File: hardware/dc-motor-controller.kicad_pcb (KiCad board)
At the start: 2 copper layers, 52.2 x 85 mm, 30 parts, among them IC1 ATMEGA88PA-P, M1 DC_motor, M2 DC_motor, M3 DC_motor, P1 Power connector, P2 ISP interface, SW1 SW_PUSH, SW2 SW_PUSH, SW3 SW_PUSH, SW4 SW_PUSH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

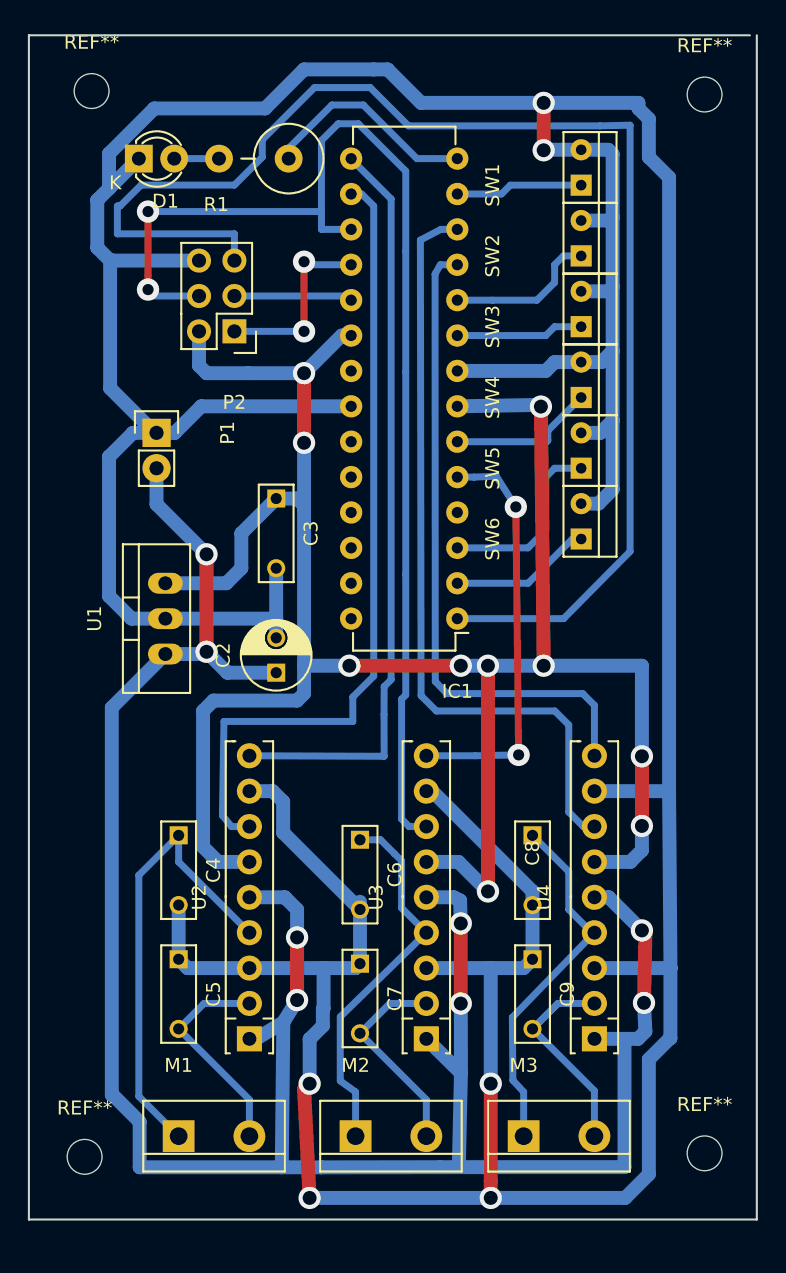
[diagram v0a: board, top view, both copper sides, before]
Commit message: Some changes after reviewing the printed circuit board
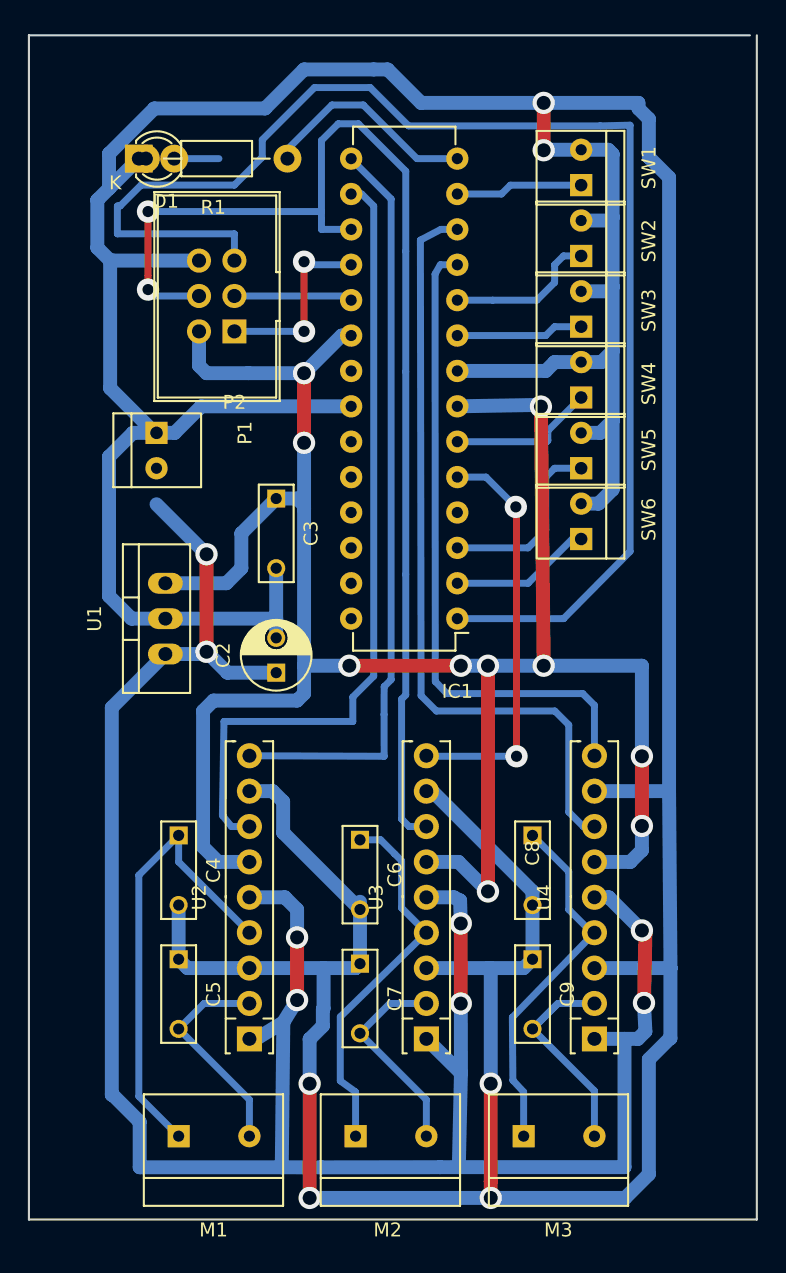
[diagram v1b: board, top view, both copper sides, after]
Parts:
- removed REF** (x4): MountingHole_2-5mm, Mounting_Holes:MountingHole_2-5mm
- M1, M2, M3: footprint Oturpe footprints:Big_green_chocolade_1x2 -> Oturpe footprints:Big_green_chocolate_1x2
- P1: footprint Socket_Strips:Socket_Strip_Straight_1x02 -> Oturpe footprints:Small_green_chocolade_1x2
- P2: footprint Pin_Headers:Pin_Header_Straight_2x03 -> Oturpe footprints:Borg_hedged_2x03
- R1: footprint Resistors_ThroughHole:Resistor_Vertical_RM5mm -> Resistors_ThroughHole:Resistor_Horizontal_RM10mm
- moved R1 2.41 mm to (114.8, 101.6)
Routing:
- net +12V: track 173.1 -> 170.5 mm

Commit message: Improved part numbering of schematic
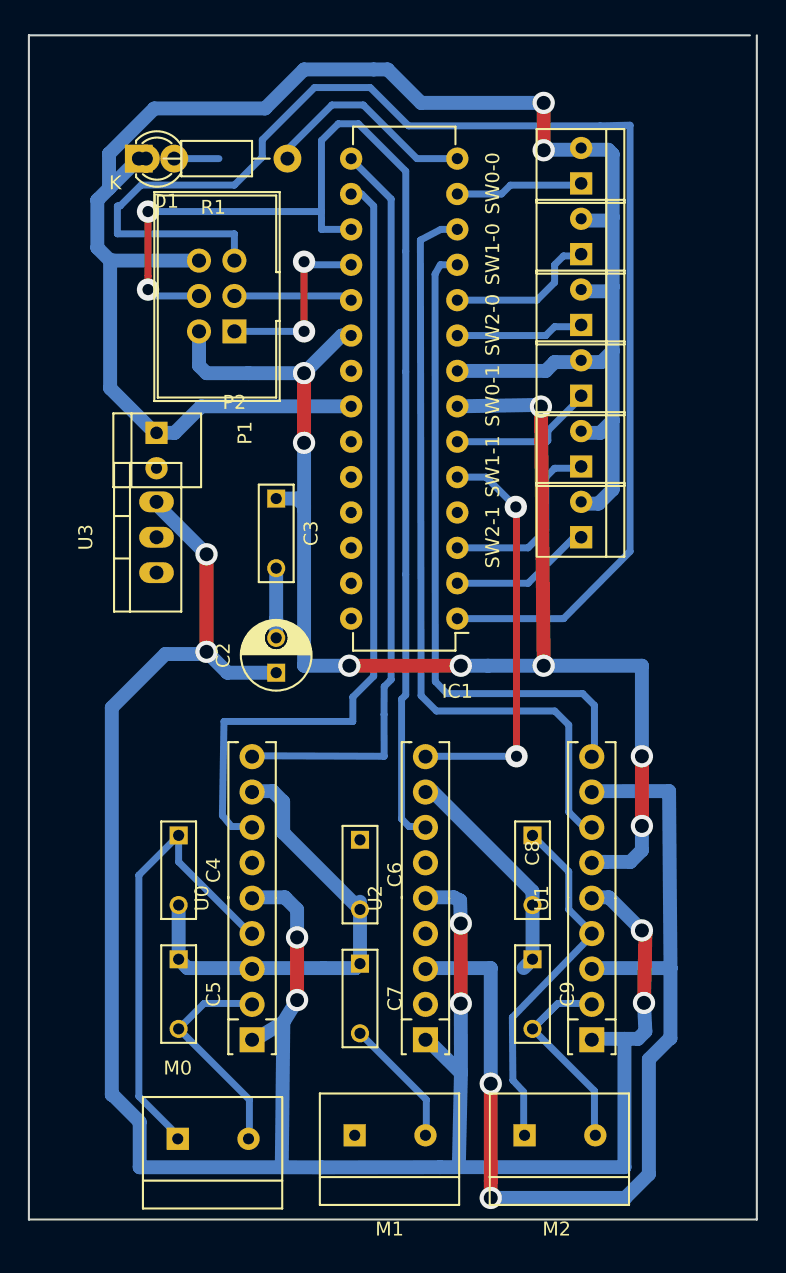
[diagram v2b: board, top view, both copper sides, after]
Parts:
- removed M3: DC_motor, Oturpe footprints:Big_green_chocolate_1x2
- removed SW1, SW2, SW3, SW4, SW5, SW6: SW_PUSH, Oturpe footprints:Small_green_chocolade_1x2
- removed U4: BA6956AN, Housings_SIP:SIP9_Housing
- added M0: DC_motor, Oturpe footprints:Big_green_chocolate_1x2, F.Cu at (106.9, 172.0)
- added SW0-0: SW_PUSH, Oturpe footprints:Small_green_chocolade_1x2, F.Cu at (135.9, 103.4)
- added SW0-1: SW_PUSH, Oturpe footprints:Small_green_chocolade_1x2, F.Cu at (135.9, 118.6)
- added SW1-0: SW_PUSH, Oturpe footprints:Small_green_chocolade_1x2, F.Cu at (135.9, 108.5)
- added SW1-1: SW_PUSH, Oturpe footprints:Small_green_chocolade_1x2, F.Cu at (135.9, 123.7)
- added SW2-0: SW_PUSH, Oturpe footprints:Small_green_chocolade_1x2, F.Cu at (135.9, 113.5)
- added SW2-1: SW_PUSH, Oturpe footprints:Small_green_chocolade_1x2, F.Cu at (135.9, 128.8)
- added U0: BA6956AN, Housings_SIP:SIP9_Housing, F.Cu at (112.3, 154.7)
- U1: value 7805 -> BA6956AN; footprint TO_SOT_Packages_THT:TO-220_Neutral123_Vertical -> Housings_SIP:SIP9_Housing
- U3: value BA6956AN -> 7805; footprint Housings_SIP:SIP9_Housing -> TO_SOT_Packages_THT:TO-220_Neutral123_Vertical
- moved U1 36.6 mm to (136.7, 154.7)
- moved U3 32.3 mm to (105.4, 128.8)
- moved M1 12.6 mm to (119.6, 171.7)
- moved U2 12.6 mm to (124.7, 154.7)
- moved M2 12.1 mm to (131.8, 171.7)
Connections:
- IC1 pad 11: Net-(IC1-Pad11) -> /M0R
- IC1 pad 12: Net-(IC1-Pad12) -> /M0F
- IC1 pad 15: Net-(IC1-Pad15) -> /M1F
- IC1 pad 16: Net-(IC1-Pad16) -> /M1R
- IC1 pad 17: Net-(IC1-Pad17) -> /M2R
- IC1 pad 5: Net-(IC1-Pad5) -> /M2R
- M1 pad 1: Net-(C4-Pad1) -> Net-(C6-Pad1)
- M1 pad 2: Net-(C5-Pad2) -> Net-(C7-Pad2)
- M2 pad 1: Net-(C6-Pad1) -> Net-(C8-Pad1)
- M2 pad 2: Net-(C7-Pad2) -> Net-(C9-Pad2)
- P2 pad 4: Net-(IC1-Pad17) -> /M2R
- U1 pad 1: +12V -> (no net)
- U1 pad 2: GND -> Net-(C7-Pad2)
- U1 pad 3: +5V -> GND
- U2 pad 1: +12V -> (no net)
- U2 pad 2: Net-(C5-Pad2) -> Net-(C9-Pad2)
- U2 pad 4: Net-(C4-Pad1) -> Net-(C8-Pad1)
- U2 pad 6: +5V -> +12V
- U2 pad 7: Net-(IC1-Pad16) -> (no net)
- U2 pad 9: Net-(IC1-Pad15) -> /M2R
- U3 pad 2: Net-(C7-Pad2) -> GND
- U3 pad 3: GND -> +5V
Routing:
- net /M2R: track 0.00 -> 116.9 mm, vias 0 -> 4
- net GND: track 380.4 -> 263.9 mm, vias 6 -> 4
- net /M0R: track 0.00 -> 93.3 mm
- net Net-(IC1-Pad17): track 87.4 -> 0.00 mm, vias 2 -> 0
- net /M0F: track 0.00 -> 58.8 mm
- net Net-(IC1-Pad16): track 57.9 -> 0.00 mm
- net /M1F: track 0.00 -> 56.8 mm
- net Net-(IC1-Pad12): track 55.5 -> 0.00 mm
- net Net-(IC1-Pad15): track 54.0 -> 0.00 mm
- net +5V: track 161.6 -> 110.8 mm, vias 10 -> 8
- net Net-(IC1-Pad11): track 47.0 -> 0.00 mm
- net Net-(IC1-Pad5): track 29.5 -> 0.00 mm, vias 2 -> 0
- net Net-(C8-Pad1): track 26.2 -> 6.86 mm
- net Net-(C6-Pad1): track 27.3 -> 19.4 mm
- net +12V: track 170.5 -> 164.6 mm
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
